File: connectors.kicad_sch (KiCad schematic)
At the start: 4 parts, among them J1 Conn_01x04_Pin, J2 Conn_01x04_Pin, J3 Conn_01x09_Pin, J4 Conn_02x03_Odd_Even

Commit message: completed footprint association
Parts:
- J1, J2: footprint (none) -> Connector_PinHeader_2.54mm:PinHeader_1x04_P2.54mm_Vertical
- J3: footprint (none) -> Connector_PinHeader_2.54mm:PinHeader_1x09_P2.54mm_Vertical
- J4: footprint (none) -> Connector_PinHeader_2.54mm:PinHeader_2x03_P2.54mm_Vertical
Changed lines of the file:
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@@
 			)
 		)
-		(property "Footprint" ""
+		(property "Footprint" "Connector_PinHeader_2.54mm:PinHeader_1x04_P2.54mm_Vertical"
 			(at 164.846 97.79 0)
 			(effects
@@
 			)
 		)
-		(property "Footprint" ""
+		(property "Footprint" "Connector_PinHeader_2.54mm:PinHeader_1x09_P2.54mm_Vertical"
 			(at 145.034 128.016 0)
 			(effects
@@
 			)
 		)
-		(property "Footprint" ""
+		(property "Footprint" "Connector_PinHeader_2.54mm:PinHeader_1x04_P2.54mm_Vertical"
 			(at 142.748 98.552 0)
 			(effects
@@
 			)
 		)
-		(property "Footprint" ""
+		(property "Footprint" "Connector_PinHeader_2.54mm:PinHeader_2x03_P2.54mm_Vertical"
 			(at 172.466 127.762 0)
 			(effects

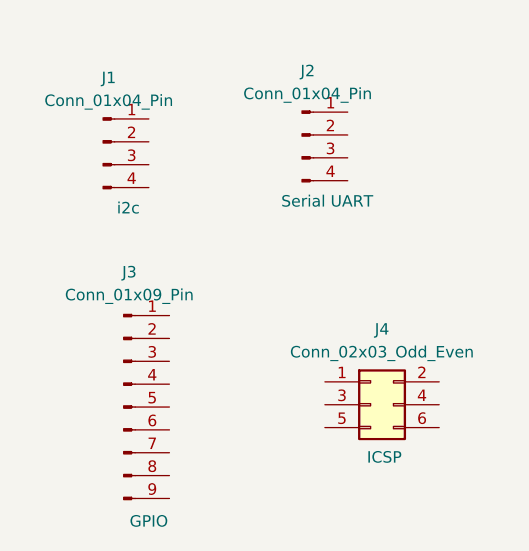
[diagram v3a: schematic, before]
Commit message: Completed the wiring including second sheet
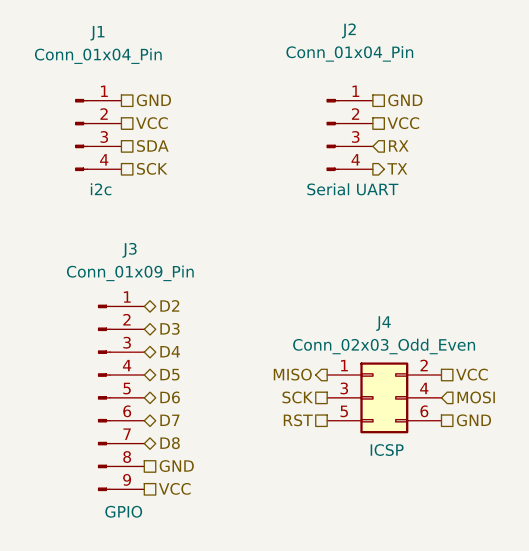
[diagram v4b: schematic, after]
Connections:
- net GND: now reaches J2.1 (Pin_1)
- net GND: now also J1.1 (Pin_1), J3.8 (Pin_8), J4.6 (Pin_6)
- net VCC: now reaches J2.2 (Pin_2)
- net VCC: now also J1.2 (Pin_2), J3.9 (Pin_9), J4.2 (Pin_2)
- net RX: now reaches J2.3 (Pin_3)
- net TX: now reaches J2.4 (Pin_4)
- net D2: now reaches J3.1 (Pin_1)
- net D3: now reaches J3.2 (Pin_2)
- net D4: now reaches J3.3 (Pin_3)
- net D5: now reaches J3.4 (Pin_4)
- net D6: now reaches J3.5 (Pin_5)
- net D7: now reaches J3.6 (Pin_6)
- net D8: now reaches J3.7 (Pin_7)
- net SDA: now reaches J1.3 (Pin_3)
- net SCK: now reaches J1.4 (Pin_4)
- net SCK: now also J4.3 (Pin_3)
- net MISO: now reaches J4.1 (Pin_1)
- net MOSI: now reaches J4.4 (Pin_4)
- net RST: now reaches J4.5 (Pin_5)
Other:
- moved on the sheet: J1, J2, J3, J4

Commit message: routing expect gnd and vcc
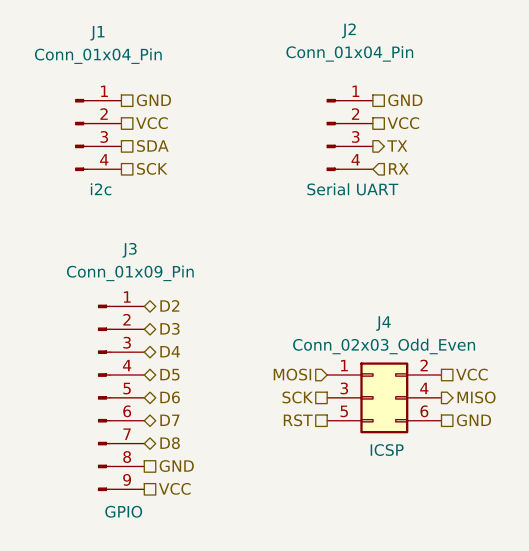
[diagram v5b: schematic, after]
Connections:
- net MISO: now also J4.4 (Pin_4); no longer J4.1 (Pin_1)
- net MOSI: now also J4.1 (Pin_1); no longer J4.4 (Pin_4)
- net RX: now also J2.4 (Pin_4); no longer J2.3 (Pin_3)
- net TX: now also J2.3 (Pin_3); no longer J2.4 (Pin_4)
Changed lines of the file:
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@@
 	(hierarchical_label "RX"
 		(shape input)
-		(at 172.72 99.06 0)
+		(at 172.72 101.6 0)
 		(effects
 			(font
@@
 	(hierarchical_label "MISO"
 		(shape output)
-		(at 167.64 124.46 180)
+		(at 180.34 127 0)
 		(effects
 			(font
 				(size 1.27 1.27)
 			)
-			(justify right)
+			(justify left)
 		)
 	)
@@
 	(hierarchical_label "TX"
 		(shape output)
-		(at 172.72 101.6 0)
+		(at 172.72 99.06 0)
 		(effects
 			(font
@@
 	(hierarchical_label "MOSI"
 		(shape input)
-		(at 180.34 127 0)
+		(at 167.64 124.46 180)
 		(effects
 			(font
 				(size 1.27 1.27)
 			)
-			(justify left)
+			(justify right)
 		)
 	)

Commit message: Fixed two defects in schematic.
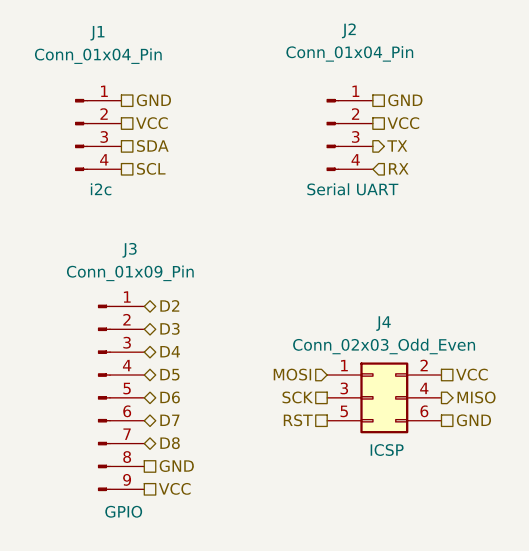
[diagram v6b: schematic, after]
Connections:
- net SCK: no longer J1.4 (Pin_4)
- new net SCL: J1.4 (Pin_4)
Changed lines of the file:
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@@
 		)
 	)
-	(hierarchical_label "SCK"
+	(hierarchical_label "SCL"
 		(shape passive)
 		(at 144.78 101.6 0)
